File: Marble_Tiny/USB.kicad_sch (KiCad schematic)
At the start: 40 parts, among them J2 USB_C_Receptacle_USB2.0_16P, Q2 XTAL_12MHZ_TXC_7A-12.000MAAJ-T, U21 FT2232HQ, U22 93C46B-I_SN, U8 TLV62565DBV

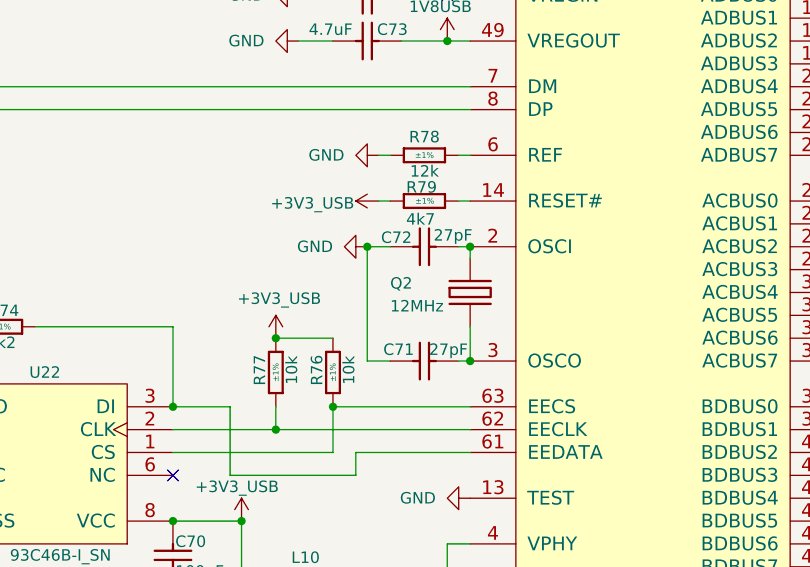
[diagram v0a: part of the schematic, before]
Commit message: connected more address lines to DDR, new board name
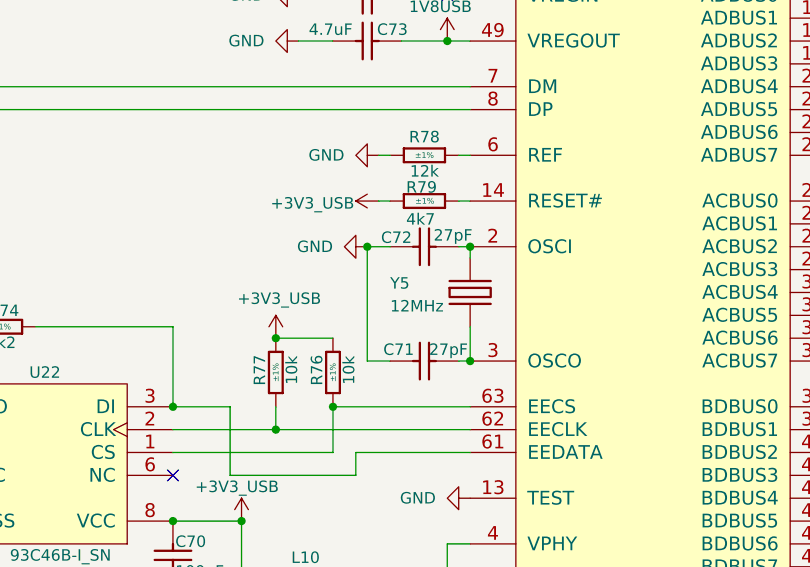
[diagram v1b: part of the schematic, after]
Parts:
- renumbered Q2 to Y5
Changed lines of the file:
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@@
 		(on_board yes)
 		(dnp no)
-		(property "Reference" "Q2"
+		(property "Reference" "Y5"
 			(at 172.72 61.214 90)
 			(effects
@@
 			(project ""
 				(path "/c2a4f786-b14c-434a-acf7-b20fb2221b0b/62565c75-62b0-4544-832f-1275174835af"
-					(reference "Q2")
+					(reference "Y5")
 					(unit 1)
 				)

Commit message: ready for the final review
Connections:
- net RTS: now reaches U21.40 (BDBUS2)
- no-connect marks 33 -> 32
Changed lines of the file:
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@@
-	)
-	(no_connect
-		(at 222.25 80.01)
 	)
 	(no_connect
@@
 		(pts
 			(xy 181.61 39.37) (xy 97.79 39.37)
+		)
+		(stroke
+			(width 0)
+			(type default)
+		)
+	)
+	(wire
+		(pts
+			(xy 222.25 80.01) (xy 242.57 80.01)
 		)
 		(stroke
@@
 	(label "USB_TCK"
 		(at 223.52 29.21 0)
+		(effects
+			(font
+				(size 1.27 1.27)
+			)
+			(justify left bottom)
+		)
+	)
+	(label "RTS"
+		(at 226.06 80.01 0)
 		(effects
 			(font
@@
 			(effects
 				(font
+					(size 1.27 1.27)
+				)
+				(justify left)
+				(hide yes)
+			)
+		)
+	)
+	(global_label "RTS"
+		(shape output)
+		(at 242.57 80.01 0)
+		(fields_autoplaced yes)
+		(effects
+			(font
+				(size 1.27 1.27)
+			)
+			(justify left)
+		)
+		(property "Intersheetrefs" "${INTERSHEET_REFS}"
+			(at 249.0023 80.01 0)
+			(effects
+				(font
